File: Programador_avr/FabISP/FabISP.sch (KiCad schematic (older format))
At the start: 14 parts

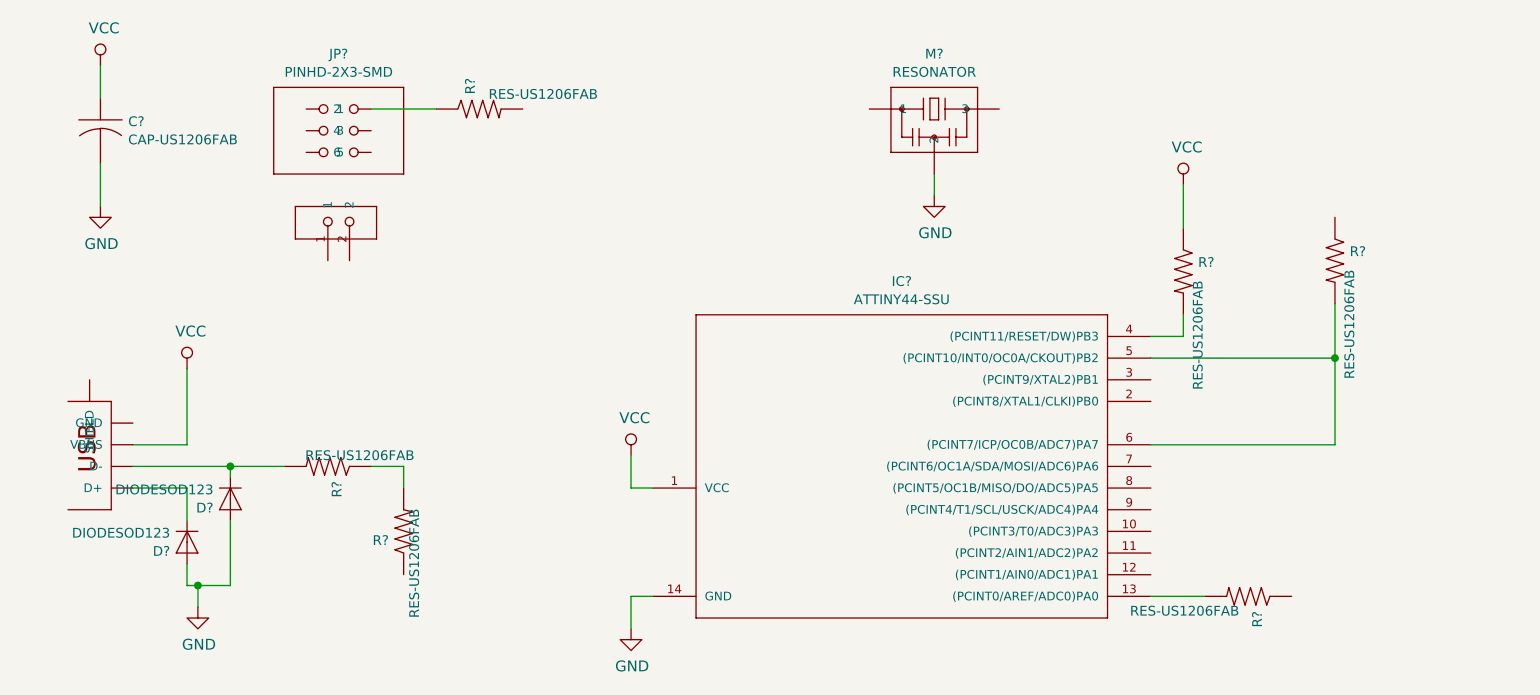
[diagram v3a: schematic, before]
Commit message: Circuito completo con huellas
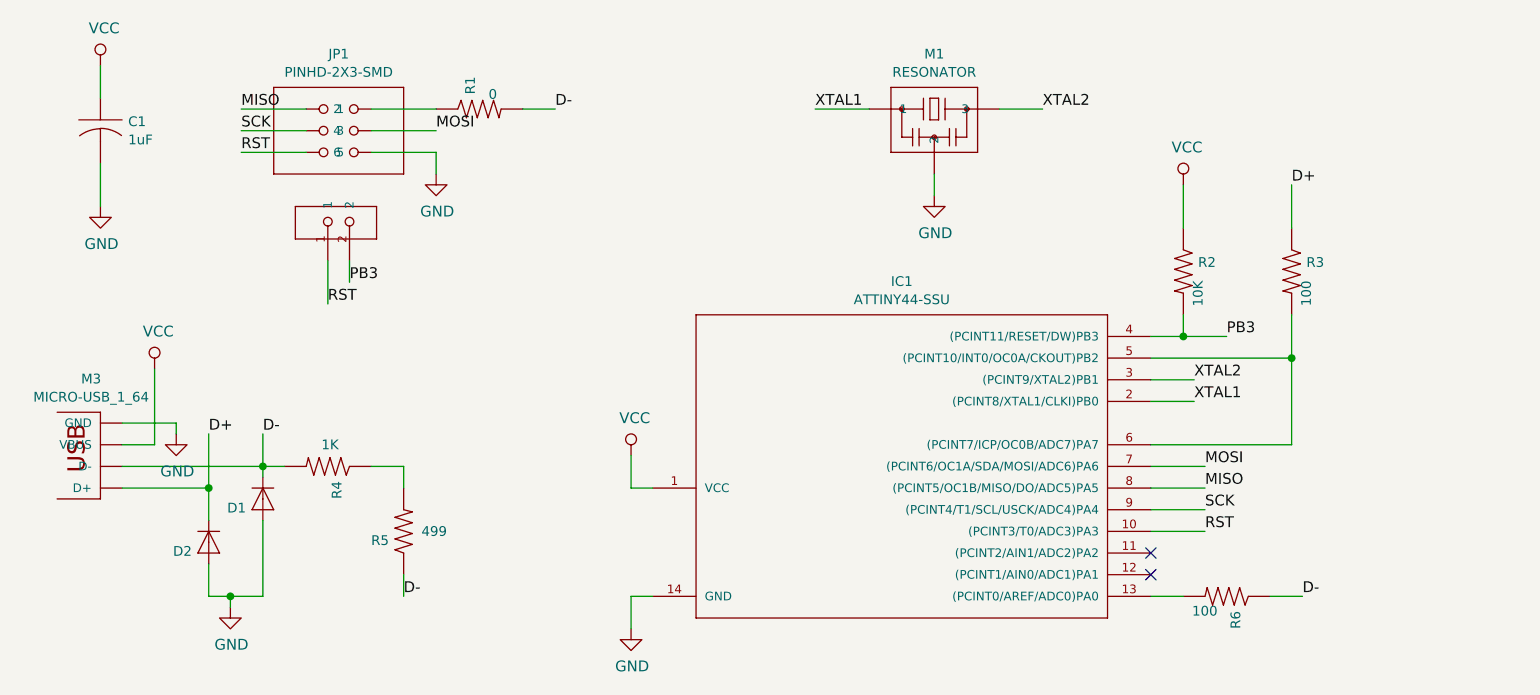
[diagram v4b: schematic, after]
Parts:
- removed M?: USB_MINIB, fab:fab-USB_MINIB, symbol fab:USB_MINIB
- added M3: MICRO-USB_1_64, fab:fab-DX4R005HJ5_64, symbol fab:MICRO-USB_1_64
- C1: renamed from C?; value CAP-US1206FAB -> 1uF
- D1, D2: renamed from D?; value DIODESOD123 -> (none)
- R1: renamed from R?; value RES-US1206FAB -> 0
- R2: renamed from R?; value RES-US1206FAB -> 10K
- R3, R6: renamed from R?; value RES-US1206FAB -> 100
- R4: renamed from R?; value RES-US1206FAB -> 1K
- R5: renamed from R?; value RES-US1206FAB -> 499
- gave numbers to parts that had none: 4
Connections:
- net GND: now also JP1.6, M3.GND
- net VCC: now also M3.VBUS
- net D+: now reaches D2.CATHODE (C)
- net D+: now also R3.1, M3.D+
- net D-: now reaches D1.CATHODE (C), R4.2
- net D-: now also R1.2, R5.1, R6.1, M3.D-
- net XTAL1: now reaches M1.1
- net XTAL1: now also IC1.2 ((PCINT8/XTAL1/CLKI)PB0)
- net XTAL2: now reaches M1.3
- net XTAL2: now also IC1.3 ((PCINT9/XTAL2)PB1)
- net MISO: now reaches JP1.1
- net MISO: now also IC1.8 ((PCINT5/OC1B/MISO/DO/ADC5)PA5)
- net SCK: now reaches JP1.3
- net SCK: now also IC1.9 ((PCINT4/T1/SCL/USCK/ADC4)PA4)
- net MOSI: now reaches JP1.4
- net MOSI: now also IC1.7 ((PCINT6/OC1A/SDA/MOSI/ADC6)PA6)
- net RST: now reaches JP1.5
- net RST: now also IC1.10 ((PCINT3/T0/ADC3)PA3), M2.1
- net PB3: now reaches IC1.4 ((PCINT11/RESET/DW)PB3), R2.2
- net PB3: now also M2.2
- no-connect marks 0 -> 2
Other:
- moved on the sheet: D1, D2, R3, R6
